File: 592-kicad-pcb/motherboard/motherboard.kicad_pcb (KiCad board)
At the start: 4 copper layers, 0 parts

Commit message: rough layout stufF
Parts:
- added C1: 100n, Capacitor_SMD:C_0603_1608Metric, F.Cu at (92.2, 148.4)
- added C10: 100n, Capacitor_SMD:C_0603_1608Metric, F.Cu at (91.0, 129.9)
- added C11: 100n, Capacitor_SMD:C_0603_1608Metric, F.Cu at (86.7, 129.9)
- added C2: 100n, Capacitor_SMD:C_0603_1608Metric, F.Cu at (103.0, 140.1)
- added C3: 1u, Capacitor_SMD:C_0603_1608Metric, F.Cu at (97.5, 137.8)
- added C5: 16p, Capacitor_SMD:C_0603_1608Metric, F.Cu at (86.7, 154.4)
- added C6: 16p, Capacitor_SMD:C_0603_1608Metric, F.Cu at (86.7, 157.6)
- added C7: 100n, Capacitor_SMD:C_0603_1608Metric, F.Cu at (87.2, 148.4)
- added C8: 1u 1206, Resistor_SMD:R_1206_3216Metric, F.Cu at (105.0, 114.0)
- added C9: 100n, Capacitor_SMD:C_0603_1608Metric, F.Cu at (99.0, 162.5)
- added J1: U.FL, Connector_Coaxial:U.FL_Hirose_U.FL-R-SMT-1_Vertical, F.Cu at (86.7, 138.9)
- added J2: U.FL, Connector_Coaxial:U.FL_Hirose_U.FL-R-SMT-1_Vertical, F.Cu at (102.0, 145.1)
- added J3: U.FL, Connector_Coaxial:U.FL_Hirose_U.FL-R-SMT-1_Vertical, F.Cu at (102.0, 135.1)
- added J4: Conn_02x06_Odd_Even, Connector_PinSocket_2.54mm:PinSocket_2x06_P2.54mm_Horizontal, B.Cu at (63.1, 125.8)
- added J5: Conn_02x06_Odd_Even, Connector_PinSocket_2.54mm:PinSocket_2x06_P2.54mm_Horizontal, B.Cu at (62.5, 148.6)
- added J6: 2.54mm jumper, Connector_PinHeader_2.54mm:PinHeader_1x03_P2.54mm_Vertical, F.Cu at (103.0, 121.5)
- added J7: Conn_02x06_Odd_Even, Connector_PinSocket_2.54mm:PinSocket_2x06_P2.54mm_Horizontal, B.Cu at (119.9, 134.7)
- added J8: Conn_02x06_Odd_Even, Connector_PinSocket_2.54mm:PinSocket_2x06_P2.54mm_Horizontal, B.Cu at (62.6, 169.3)
- added J9: Conn_02x06_Odd_Even, Connector_PinSocket_2.54mm:PinSocket_2x06_P2.54mm_Horizontal, B.Cu at (119.4, 155.2)
- added JP1: Jumper_2_Small_Bridged, Jumper:SolderJumper-2_P1.3mm_Bridged_RoundedPad1.0x1.5mm, F.Cu at (84.7, 154.2)
- added JP2: Jumper_2_Small_Bridged, Jumper:SolderJumper-2_P1.3mm_Bridged_RoundedPad1.0x1.5mm, F.Cu at (84.7, 157.8)
- added R1: 1M, Resistor_SMD:R_0603_1608Metric, F.Cu at (107.5, 136.1)
- added R10: 100k, Resistor_SMD:R_0603_1608Metric, F.Cu at (73.0, 122.0)
- added R11: 100k, Resistor_SMD:R_0603_1608Metric, F.Cu at (73.0, 124.5)
- added R12: 4k, Resistor_SMD:R_0603_1608Metric, F.Cu at (80.0, 166.5)
- added R13: 4k, Resistor_SMD:R_0603_1608Metric, F.Cu at (82.5, 166.5)
- added R14: 10k, Resistor_SMD:R_0603_1608Metric, F.Cu at (91.0, 127.9)
- added R15: 10k, Resistor_SMD:R_0603_1608Metric, F.Cu at (86.7, 127.9)
- added R16: 1M, Resistor_SMD:R_0603_1608Metric, F.Cu at (105.5, 127.7)
- added R17: 100k, Resistor_SMD:R_0603_1608Metric, F.Cu at (73.0, 127.0)
- added R18: 100k, Resistor_SMD:R_0603_1608Metric, F.Cu at (72.5, 114.5)
- added R19: 100k, Resistor_SMD:R_0603_1608Metric, F.Cu at (73.2, 141.0)
- added R2: 1M, Resistor_SMD:R_0603_1608Metric, F.Cu at (107.5, 144.1)
- added R20: 4k, Resistor_SMD:R_0603_1608Metric, F.Cu at (85.0, 166.5)
- added R21: 100k, Resistor_SMD:R_0603_1608Metric, F.Cu at (87.5, 166.5)
- added R22: 100k, Resistor_SMD:R_0603_1608Metric, F.Cu at (90.0, 166.5)
- added R23: 100k, Resistor_SMD:R_0603_1608Metric, F.Cu at (73.2, 143.5)
- added R24: 100k, Resistor_SMD:R_0603_1608Metric, F.Cu at (73.2, 146.0)
- added R25: 4k, Resistor_SMD:R_0603_1608Metric, F.Cu at (92.5, 166.5)
- added R26: 100k, Resistor_SMD:R_0603_1608Metric, F.Cu at (73.2, 148.5)
- added R27: 100k, Resistor_SMD:R_0603_1608Metric, F.Cu at (72.7, 136.5)
- added R28: 1M, Resistor_SMD:R_0603_1608Metric, F.Cu at (113.2, 142.0)
- added R29: 1M, Resistor_SMD:R_0603_1608Metric, F.Cu at (113.2, 139.5)
- added R3: 10, Resistor_SMD:R_0603_1608Metric, F.Cu at (87.7, 143.4)
- added R32: 100k, Resistor_SMD:R_0603_1608Metric, F.Cu at (89.7, 138.4)
- added R4: 10, Resistor_SMD:R_0603_1608Metric, F.Cu at (89.7, 143.4)
- added R5: 10, Resistor_SMD:R_0603_1608Metric, F.Cu at (92.2, 144.9)
- added R6: 10k, Resistor_SMD:R_0603_1608Metric, F.Cu at (104.5, 118.5)
- added R7: 10k, Resistor_SMD:R_0603_1608Metric, F.Cu at (99.0, 159.0)
- added R8: 100k, Resistor_SMD:R_0603_1608Metric, F.Cu at (72.5, 118.0)
- added R9: 100k, Resistor_SMD:R_0603_1608Metric, F.Cu at (72.8, 139.0)
- added SW1: C318884, Button_Switch_SMD:SW_Push_1P1T_XKB_TS-1187A, F.Cu at (103.0, 161.5)
- added U1: SN74LVC1G3157DBVR, Package_TO_SOT_SMD:SOT-23-6, F.Cu at (86.7, 133.9)
- added U2: SMXS-04K, 592-partslib:SMXS-04K-TP, F.Cu at (88.2, 120.4)
- added U3: SN74LVC1G3157DBVR, Package_TO_SOT_SMD:SOT-23-6, F.Cu at (91.1, 134.0)
- added U4: OPA2328DR, Package_SO:VSSOP-8_3x3mm_P0.65mm, F.Cu at (105.5, 140.1)
- added U5: 74LVC1T45GW, Package_TO_SOT_SMD:SOT-363_SC-70-6, F.Cu at (103.2, 127.6)
- added U6: 74LVC1T45GW, Package_TO_SOT_SMD:SOT-363_SC-70-6, F.Cu at (104.6, 154.9)
- added U8: 74LVC1T45GW, Package_TO_SOT_SMD:SOT-363_SC-70-6, F.Cu at (92.2, 138.4)
- added U9: SN74LVC1G14DBV, Package_TO_SOT_SMD:SOT-23-5, F.Cu at (101.0, 155.0)
- added Y1: Si5351A, Package_SO:MSOP-10_3x3mm_P0.5mm, F.Cu at (89.7, 148.4)
- added Y2: NX3225GA-25.000M-STD-CRG-2, Crystal:Crystal_SMD_3225-4Pin_3.2x2.5mm, F.Cu at (89.3, 155.0)
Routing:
- net /CHIP_FS_EXT: track 0.00 -> 12.1 mm
- net /clock_sources/FS_EXT_GEN: track 0.00 -> 9.81 mm
- net /MCU_GPIO_FS_SEL: track 0.00 -> 8.94 mm
- net /MCU_GPIO_NFCCLK_SEL: track 0.00 -> 8.85 mm
- net /CHIP_ext_clk_dig: track 0.00 -> 8.37 mm
- net /ANA_MUX_OUT_2_BUF: track 0.00 -> 5.11 mm
- net /ANA_MUX_OUT_1_BUF: track 0.00 -> 4.15 mm
- net /clock_sources/FS_EXT_AUX: track 0.00 -> 3.90 mm
- net Net-(Y1-CLK0): track 0.00 -> 2.48 mm
- net Net-(Y1-CLK1): track 0.00 -> 2.27 mm
- net /clock_sources/EXT_CLK_DIG_GEN: track 0.00 -> 1.79 mm
- net /CHIP_NFC_AFE_TDO_EXT: track 0.00 -> 1.77 mm

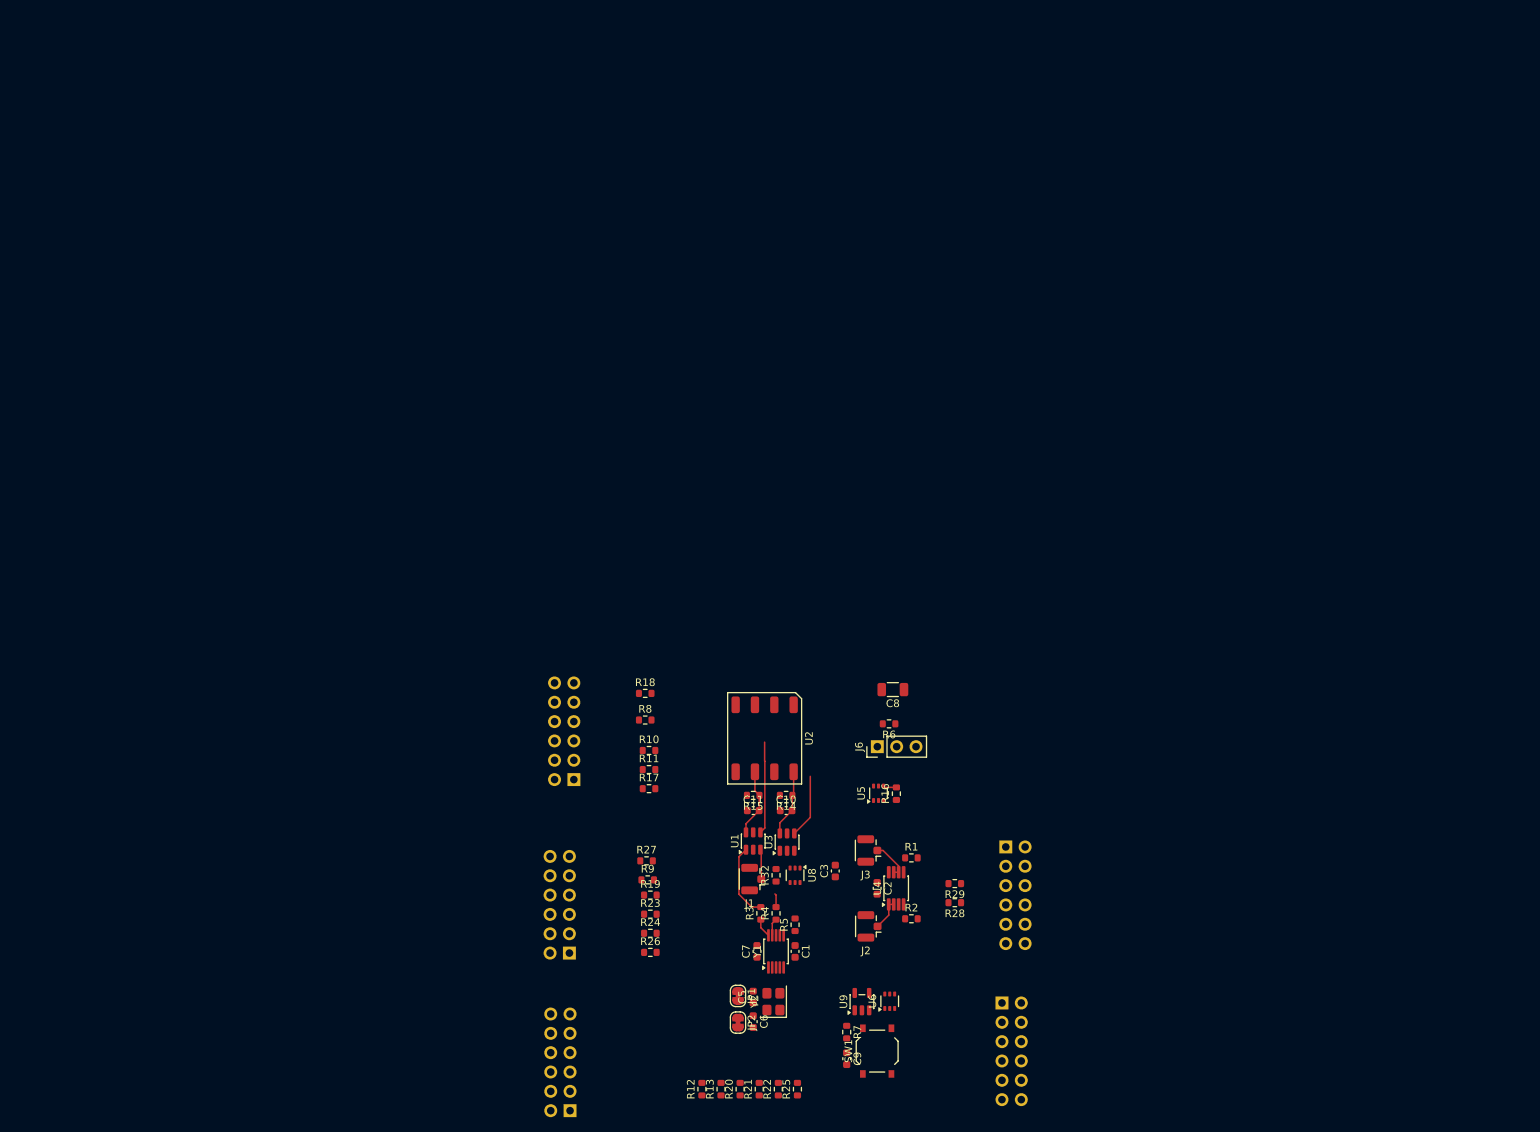
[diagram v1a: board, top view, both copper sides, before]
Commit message: add JLC part num for parts, footprints
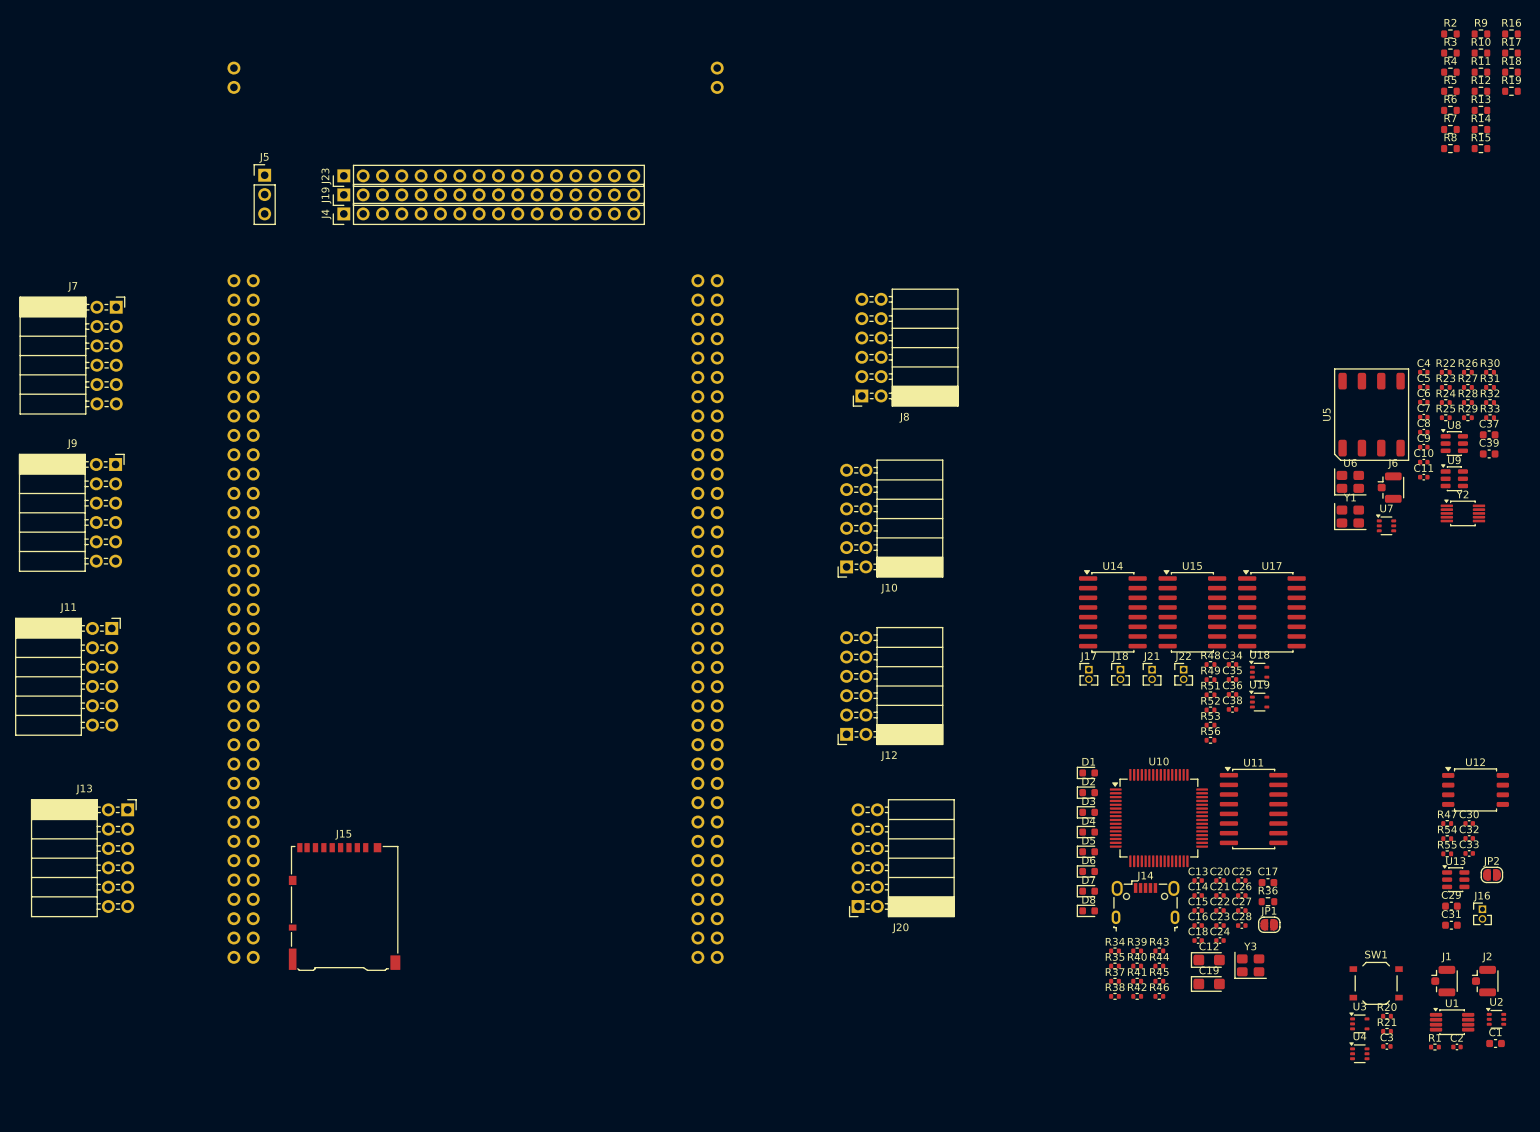
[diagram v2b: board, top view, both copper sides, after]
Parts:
- removed J3: U.FL, Connector_Coaxial:U.FL_Hirose_U.FL-R-SMT-1_Vertical
- added C12: 4.7u, Capacitor_Tantalum_SMD:CP_EIA-3216-18_Kemet-A, F.Cu at (146.6, 149.5)
- added C13: 10p, Capacitor_SMD:C_0402_1005Metric, F.Cu at (145.1, 139.1)
- added C14: 10p, Capacitor_SMD:C_0402_1005Metric, F.Cu at (145.1, 141.1)
- added C15: 100n, Capacitor_SMD:C_0402_1005Metric, F.Cu at (145.1, 143.0)
- added C16: 100n, Capacitor_SMD:C_0402_1005Metric, F.Cu at (145.1, 145.0)
- added C17: 3.3u, Capacitor_SMD:C_0603_1608Metric, F.Cu at (154.3, 139.4)
- added C18: 10n, Capacitor_SMD:C_0402_1005Metric, F.Cu at (145.1, 147.0)
- added C19: 4.7u, Capacitor_Tantalum_SMD:CP_EIA-3216-18_Kemet-A, F.Cu at (146.6, 152.7)
- added C20: 100n, Capacitor_SMD:C_0402_1005Metric, F.Cu at (148.0, 139.1)
- added C21: 100n, Capacitor_SMD:C_0402_1005Metric, F.Cu at (148.0, 141.1)
- added C22: 100n, Capacitor_SMD:C_0402_1005Metric, F.Cu at (148.0, 143.0)
- added C23: 100n, Capacitor_SMD:C_0402_1005Metric, F.Cu at (148.0, 145.0)
- added C24: 100n, Capacitor_SMD:C_0402_1005Metric, F.Cu at (148.0, 147.0)
- added C25: 100n, Capacitor_SMD:C_0402_1005Metric, F.Cu at (150.9, 139.1)
- added C26: 100n, Capacitor_SMD:C_0402_1005Metric, F.Cu at (150.9, 141.1)
- added C27: 100n, Capacitor_SMD:C_0402_1005Metric, F.Cu at (150.9, 143.0)
- added C28: 100n, Capacitor_SMD:C_0402_1005Metric, F.Cu at (150.9, 145.0)
- added C29: 1u, Capacitor_SMD:C_0603_1608Metric, F.Cu at (178.4, 142.4)
- added C30: 100n, Capacitor_SMD:C_0402_1005Metric, F.Cu at (180.8, 131.6)
- added C31: 1u, Capacitor_SMD:C_0603_1608Metric, F.Cu at (178.4, 145.0)
- added C32: 100n, Capacitor_SMD:C_0402_1005Metric, F.Cu at (180.8, 133.6)
- added C33: 100n, Capacitor_SMD:C_0402_1005Metric, F.Cu at (180.8, 135.5)
- added C34: 100n, Capacitor_SMD:C_0402_1005Metric, F.Cu at (149.7, 110.7)
- added C35: 100n, Capacitor_SMD:C_0402_1005Metric, F.Cu at (149.7, 112.7)
- added C36: 100n, Capacitor_SMD:C_0402_1005Metric, F.Cu at (149.7, 114.6)
- added C37: 1u, Capacitor_SMD:C_0603_1608Metric, F.Cu at (183.4, 80.5)
- added C38: 100n, Capacitor_SMD:C_0402_1005Metric, F.Cu at (149.7, 116.6)
- added C39: 1u, Capacitor_SMD:C_0603_1608Metric, F.Cu at (183.4, 83.0)
- added C4: 16p, Capacitor_SMD:C_0402_1005Metric, F.Cu at (174.8, 72.3)
- added D1: d_white, Diode_SMD:D_0603_1608Metric, F.Cu at (130.8, 125.0)
- added D2: d_white, Diode_SMD:D_0603_1608Metric, F.Cu at (130.8, 127.5)
- added D3: d_white, Diode_SMD:D_0603_1608Metric, F.Cu at (130.8, 130.1)
- added D4: d_white, Diode_SMD:D_0603_1608Metric, F.Cu at (130.8, 132.7)
- added D5: d_red, Diode_SMD:D_0603_1608Metric, F.Cu at (130.8, 135.3)
- added D6: d_red, Diode_SMD:D_0603_1608Metric, F.Cu at (130.8, 137.9)
- added D7: d_red, Diode_SMD:D_0603_1608Metric, F.Cu at (130.8, 140.5)
- added D8: d_red, Diode_SMD:D_0603_1608Metric, F.Cu at (130.8, 143.1)
- added J10: Conn_02x06_Odd_Even, Connector_PinSocket_2.54mm:PinSocket_2x06_P2.54mm_Horizontal, F.Cu at (99.0, 97.9)
- added J11: Conn_02x06_Odd_Even, Connector_PinSocket_2.54mm:PinSocket_2x06_P2.54mm_Horizontal, F.Cu at (2.42, 106.0)
- added J12: Conn_02x06_Odd_Even, Connector_PinSocket_2.54mm:PinSocket_2x06_P2.54mm_Horizontal, F.Cu at (99.0, 119.9)
- added J13: Conn_02x06_Odd_Even, Connector_PinSocket_2.54mm:PinSocket_2x06_P2.54mm_Horizontal, F.Cu at (4.50, 129.8)
- added J14: USB_B_Micro, Connector_USB:USB_Micro-B_Wuerth_629105150521, F.Cu at (138.2, 142.0)
- added J15: Micro_SD_Card, Connector_Card:microSD_HC_Hirose_DM3AT-SF-PEJM5, F.Cu at (33.0, 142.5)
- added J16: Conn_02x01, Connector_PinHeader_1.27mm:PinHeader_1x02_P1.27mm_Vertical, F.Cu at (182.5, 142.9)
- added J17: Conn_02x01, Connector_PinHeader_1.27mm:PinHeader_1x02_P1.27mm_Vertical, F.Cu at (130.8, 111.4)
- added J18: Conn_02x01, Connector_PinHeader_1.27mm:PinHeader_1x02_P1.27mm_Vertical, F.Cu at (134.9, 111.4)
- added J19: Conn_01x16, Connector_PinHeader_2.54mm:PinHeader_1x16_P2.54mm_Vertical, F.Cu at (32.9, 49.0)
- added J20: Conn_02x06_Odd_Even, Connector_PinSocket_2.54mm:PinSocket_2x06_P2.54mm_Horizontal, F.Cu at (100.5, 142.5)
- added J21: Conn_02x01, Connector_PinHeader_1.27mm:PinHeader_1x02_P1.27mm_Vertical, F.Cu at (139.1, 111.4)
- added J22: Conn_02x01, Connector_PinHeader_1.27mm:PinHeader_1x02_P1.27mm_Vertical, F.Cu at (143.2, 111.4)
- added J23: Conn_01x16, Connector_PinHeader_2.54mm:PinHeader_1x16_P2.54mm_Vertical, F.Cu at (32.9, 46.5)
- added R30: 10k, Resistor_SMD:R_0402_1005Metric, F.Cu at (183.5, 72.3)
- added R31: 10k, Resistor_SMD:R_0402_1005Metric, F.Cu at (183.5, 74.3)
- added R33: 10k, Resistor_SMD:R_0402_1005Metric, F.Cu at (183.5, 78.3)
- added R34: 4.7k, Resistor_SMD:R_0402_1005Metric, F.Cu at (134.2, 148.3)
- added R35: 10k, Resistor_SMD:R_0402_1005Metric, F.Cu at (134.2, 150.3)
- added R36: 12k <1%, Resistor_SMD:R_0603_1608Metric, F.Cu at (154.3, 141.9)
- added R37: 1k, Resistor_SMD:R_0402_1005Metric, F.Cu at (134.2, 152.3)
- added R38: 150, Resistor_SMD:R_0402_1005Metric, F.Cu at (134.2, 154.3)
- added R39: 150, Resistor_SMD:R_0402_1005Metric, F.Cu at (137.1, 148.3)
- added R40: 150, Resistor_SMD:R_0402_1005Metric, F.Cu at (137.1, 150.3)
- added R41: 150, Resistor_SMD:R_0402_1005Metric, F.Cu at (137.1, 152.3)
- added R42: 330, Resistor_SMD:R_0402_1005Metric, F.Cu at (137.1, 154.3)
- added R43: 330, Resistor_SMD:R_0402_1005Metric, F.Cu at (140.0, 148.3)
- added R44: 330, Resistor_SMD:R_0402_1005Metric, F.Cu at (140.0, 150.3)
- added R45: 330, Resistor_SMD:R_0402_1005Metric, F.Cu at (140.0, 152.3)
- added R46: 10k, Resistor_SMD:R_0402_1005Metric, F.Cu at (140.0, 154.3)
- added R47: 10k, Resistor_SMD:R_0402_1005Metric, F.Cu at (177.9, 131.6)
- added R48: 10k, Resistor_SMD:R_0402_1005Metric, F.Cu at (146.8, 110.7)
- added R49: 10k, Resistor_SMD:R_0402_1005Metric, F.Cu at (146.8, 112.7)
- added R51: 10k, Resistor_SMD:R_0402_1005Metric, F.Cu at (146.8, 114.7)
- added R52: 10k, Resistor_SMD:R_0402_1005Metric, F.Cu at (146.8, 116.7)
- added R53: 10k, Resistor_SMD:R_0402_1005Metric, F.Cu at (146.8, 118.7)
- added R54: 10k, Resistor_SMD:R_0402_1005Metric, F.Cu at (177.9, 133.6)
- added R55: 10k, Resistor_SMD:R_0402_1005Metric, F.Cu at (177.9, 135.6)
- added R56: 10k, Resistor_SMD:R_0402_1005Metric, F.Cu at (146.8, 120.7)
- added U10: FT4232H, Package_QFP:LQFP-64_10x10mm_P0.5mm, F.Cu at (140.0, 130.9)
- added U11: 74HC595, Package_SO:SOIC-16W_5.3x10.2mm_P1.27mm, F.Cu at (152.4, 129.7)
- added U12: W25Q32JVSS, Package_SO:SOIC-8_5.3x5.3mm_P1.27mm, F.Cu at (181.6, 127.2)
- added U13: SN74LVC1G3157DBVR, Package_TO_SOT_SMD:SOT-23-6, F.Cu at (179.0, 139.0)
- added U14: 74CBTLV3257, Package_SO:SOIC-16W_5.3x10.2mm_P1.27mm, F.Cu at (133.9, 103.8)
- added U15: 74CBTLV3257, Package_SO:SOIC-16W_5.3x10.2mm_P1.27mm, F.Cu at (144.4, 103.8)
- added U16: NUCLEO144-H743ZI, Module:ST_Morpho_Connector_144_STLink, B.Cu at (82.0, 60.3)
- added U17: 74CBTLV3257, Package_SO:SOIC-16W_5.3x10.2mm_P1.27mm, F.Cu at (154.8, 103.8)
- added U18: SN74LVC1G14DBV, Package_TO_SOT_SMD:SOT-353_SC-70-5, F.Cu at (153.2, 111.7)
- added U19: SN74LVC1G14DBV, Package_TO_SOT_SMD:SOT-353_SC-70-5, F.Cu at (153.2, 115.6)
- added U7: 74LVC1T45GW, Package_TO_SOT_SMD:SOT-363_SC-70-6, F.Cu at (169.9, 92.5)
- added Y3: X322512MSB4SI, Crystal:Crystal_SMD_3225-4Pin_3.2x2.5mm, F.Cu at (152.0, 150.2)
- C1: value 100n -> 1u
- C10, C2, C5, C7, C9: footprint Capacitor_SMD:C_0603_1608Metric -> Capacitor_SMD:C_0402_1005Metric
- C11: value 100n -> 10n; footprint Capacitor_SMD:C_0603_1608Metric -> Capacitor_SMD:C_0402_1005Metric
- C3: value 1u -> 100n; footprint Capacitor_SMD:C_0603_1608Metric -> Capacitor_SMD:C_0402_1005Metric
- C6: value 16p -> 100n; footprint Capacitor_SMD:C_0603_1608Metric -> Capacitor_SMD:C_0402_1005Metric
- C8: value 1u 1206 -> 100n; footprint Resistor_SMD:R_1206_3216Metric -> Capacitor_SMD:C_0402_1005Metric
- J4: value Conn_02x06_Odd_Even -> Conn_01x16; footprint Connector_PinSocket_2.54mm:PinSocket_2x06_P2.54mm_Horizontal -> Connector_PinHeader_2.54mm:PinHeader_1x16_P2.54mm_Vertical; moved to F.Cu
- J5: value Conn_02x06_Odd_Even -> 2.54mm jumper; footprint Connector_PinSocket_2.54mm:PinSocket_2x06_P2.54mm_Horizontal -> Connector_PinHeader_2.54mm:PinHeader_1x03_P2.54mm_Vertical; moved to F.Cu
- J6: value 2.54mm jumper -> U.FL; footprint Connector_PinHeader_2.54mm:PinHeader_1x03_P2.54mm_Vertical -> Connector_Coaxial:U.FL_Hirose_U.FL-R-SMT-1_Vertical
- J7, J8, J9: moved to F.Cu
- JP1, JP2: value Jumper_2_Small_Bridged -> solderjump; footprint Jumper:SolderJumper-2_P1.3mm_Bridged_RoundedPad1.0x1.5mm -> Jumper:SolderJumper-2_P1.3mm_Open_RoundedPad1.0x1.5mm
- R1, R21: footprint Resistor_SMD:R_0603_1608Metric -> Resistor_SMD:R_0402_1005Metric
- R10, R11, R17, R18, R19, R8, R9: value 100k -> 10k
- R12, R13: value 4k -> 10k
- R16: value 1M -> 10k
- R2: value 1M -> 10M
- R20: value 4k -> 10k; footprint Resistor_SMD:R_0603_1608Metric -> Resistor_SMD:R_0402_1005Metric
- R22, R23, R27, R32: value 100k -> 10k; footprint Resistor_SMD:R_0603_1608Metric -> Resistor_SMD:R_0402_1005Metric
- R24, R26: value 100k -> 10; footprint Resistor_SMD:R_0603_1608Metric -> Resistor_SMD:R_0402_1005Metric
- R25: value 4k -> 10; footprint Resistor_SMD:R_0603_1608Metric -> Resistor_SMD:R_0402_1005Metric
- R28, R29: value 1M -> 10k; footprint Resistor_SMD:R_0603_1608Metric -> Resistor_SMD:R_0402_1005Metric
- R3, R4, R5: value 10 -> 10M
- R6, R7: value 10k -> 2k
- U1: value SN74LVC1G3157DBVR -> OPA2328DGKR; footprint Package_TO_SOT_SMD:SOT-23-6 -> Package_SO:VSSOP-8_3x3mm_P0.65mm
- U2: value SMXS-04K -> 74LVC1T45GW; footprint 592-partslib:SMXS-04K-TP -> Package_TO_SOT_SMD:SOT-363_SC-70-6
- U3: value SN74LVC1G3157DBVR -> SN74LVC1G14DBV; footprint Package_TO_SOT_SMD:SOT-23-6 -> Package_TO_SOT_SMD:SOT-353_SC-70-5
- U4: value OPA2328DR -> 74LVC1T45GW; footprint Package_SO:VSSOP-8_3x3mm_P0.65mm -> Package_TO_SOT_SMD:SOT-363_SC-70-6
- U5: value 74LVC1T45GW -> SMXS-04K; footprint Package_TO_SOT_SMD:SOT-363_SC-70-6 -> 592-partslib:SMXS-04K-TP
- U6: value 74LVC1T45GW -> SX3M10.000B10F20TNN; footprint Package_TO_SOT_SMD:SOT-363_SC-70-6 -> Crystal:Crystal_SMD_3225-4Pin_3.2x2.5mm
- U8: value 74LVC1T45GW -> SN74LVC1G3157DBVR; footprint Package_TO_SOT_SMD:SOT-363_SC-70-6 -> Package_TO_SOT_SMD:SOT-23-6
- U9: value SN74LVC1G14DBV -> SN74LVC1G3157DBVR; footprint Package_TO_SOT_SMD:SOT-23-5 -> Package_TO_SOT_SMD:SOT-23-6
- Y1: value Si5351A -> NX3225GA-25.000M-STD-CRG-2; footprint Package_SO:MSOP-10_3x3mm_P0.5mm -> Crystal:Crystal_SMD_3225-4Pin_3.2x2.5mm
- Y2: value NX3225GA-25.000M-STD-CRG-2 -> Si5351A; footprint Crystal:Crystal_SMD_3225-4Pin_3.2x2.5mm -> Package_SO:MSOP-10_3x3mm_P0.5mm
- moved R12 166.3 mm to (182.3, 35.4), turned to 0 degrees
- moved R13 162.8 mm to (182.3, 37.9), turned to 0 degrees
- moved R9 156.0 mm to (182.3, 27.9)
- moved R19 154.8 mm to (186.3, 35.4)
- moved R17 148.9 mm to (186.3, 30.4)
- moved R3 144.9 mm to (178.3, 30.4), turned to 0 degrees
- moved R7 142.7 mm to (178.3, 40.4), turned to 0 degrees
- moved R10 142.6 mm to (182.3, 30.4)
- moved R11 142.6 mm to (182.3, 32.9)
- moved R4 141.7 mm to (178.3, 32.9), turned to 0 degrees
- moved R18 140.1 mm to (186.3, 32.9)
- moved R5 139.3 mm to (178.3, 35.4), turned to 0 degrees
- moved J7 136.7 mm to (3.00, 63.8), turned to 0 degrees
- moved J9 136.3 mm to (2.92, 84.4), turned to 0 degrees
- moved R2 136.1 mm to (178.3, 27.9)
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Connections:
- C1 pad 1: +1V8 -> +3V3
- C10 pad 2: /MCU_GPIO_NFCCLK_SEL -> /motherboard_top/clock_sources/FS_EXT_SEL
- C11 pad 1: GND -> +3V3
- C11 pad 2: /MCU_GPIO_FS_SEL -> GND
- C3 pad 1: +3V3 -> /motherboard_top/chip_support_misc/GPIO_RESET_EXT
- C5 pad 1: Net-(JP1-B) -> Net-(Y2-XB)
- C6 pad 1: Net-(JP2-A) -> +3V3
- C7 pad 1: +3V3 -> GND
- C7 pad 2: GND -> /motherboard_top/clock_sources/EXT_CLK_DIG_SEL
- C8 pad 1: /CHIP_VRECT_OUT_EXT -> +1V8
- C9 pad 1: /MCU_GPIO_RESET_AFE -> GND
- C9 pad 2: GND -> /motherboard_top/clock_sources/CARAVEL_CLK_SEL
- J1 pad 1: /clock_sources/FS_EXT_AUX -> /motherboard_top/ADC_chip_ana_mux_out_1
- J2 pad 1: /ANA_MUX_OUT_1_BUF -> /motherboard_top/ADC_chip_ana_mux_out_2
- J4 pad 1: /CHIP_TRST_EXT -> /motherboard_top/mgmt_debug
- J4 pad 10: GND -> /motherboard_top/chip_connection/MGMT_flash2_sck
- J4 pad 11: +3V3 -> /motherboard_top/chip_connection/MGMT_flash2_io0
- J4 pad 12: GND -> /motherboard_top/chip_connection/MGMT_flash2_io1
- J4 pad 2: /CHIP_TMS_EXT -> /motherboard_top/mgmt_sdo
- J4 pad 3: /CHIP_TCK_EXT -> /motherboard_top/mgmt_sdi
- J4 pad 4: /CHIP_TDI_EXT -> /motherboard_top/mgmt_csb
- J4 pad 5: /CHIP_tdo -> /motherboard_top/mgmt_sck
- J4 pad 6: /CHIP_tdo2 -> /motherboard_top/UART_mgmt_uart_rx
- J4 pad 7: /CHIP_ext_reset_dig -> /motherboard_top/UART_mgmt_uart_tx
- J4 pad 8: GND -> /motherboard_top/chip_connection/MGMT_irq
- J4 pad 9: GND -> /motherboard_top/chip_connection/MGMT_flash2_csb
- J5 pad 1: /CHIP_jtag_TDO -> /motherboard_top/anamisc_vref_ext_in
- J5 pad 2: /CHIP_jtag_TMS -> /motherboard_top/chip_nfc_vref
- J5 pad 3: /CHIP_jtag_TCK -> /motherboard_top/chip_support_misc/VREF_DAC_OUT
- J6 pad 1: /VREF_EXT_IN -> /motherboard_top/clock_sources/fs_ext_aux
- J6 pad 2: /CHIP_VREF_EXT -> GND
- J7 pad 1: /CHIP_i2c_0_sda -> +1V8
- J7 pad 10: /VREF_EXT_IN -> GND
- J7 pad 12: GND -> +3V3
- J7 pad 2: /ANA_MUX_OUT_1_BUF -> /motherboard_top/anamisc_vref_ext_in
- J7 pad 3: /CHIP_i2c_0_scl -> /motherboard_top/ADC_chip_ana_mux_out_1
- J7 pad 4: /ANA_MUX_OUT_2_BUF -> /motherboard_top/chip_nfc_jtag_tdi
- J7 pad 5: GND -> /motherboard_top/ADC_chip_ana_mux_out_2
- J7 pad 6: /NFC_AFE_TDO_EXT_BUF -> /motherboard_top/GPIO_chip_nfc_ext_reset_dig
- J7 pad 7: GND -> /motherboard_top/GPIO_chip_nfc_afe_tdo_ext
- J7 pad 8: /CHIP_VRECT_OUT_EXT -> /motherboard_top/chip_nfc_vrect_out
- J7 pad 9: +1V8 -> GND
- J8 pad 1: unconnected-(J8-Pin_1-Pad1) -> /motherboard_top/rck_mem_cs
- J8 pad 10: unconnected-(J8-Pin_10-Pad10) -> GND
- J8 pad 11: unconnected-(J8-Pin_11-Pad11) -> +3V3
- J8 pad 12: unconnected-(J8-Pin_12-Pad12) -> +3V3
- J8 pad 3: unconnected-(J8-Pin_3-Pad3) -> /motherboard_top/rck_mem_mosi_io0
- J8 pad 5: unconnected-(J8-Pin_5-Pad5) -> /motherboard_top/rck_mem_miso_i01
- J8 pad 6: unconnected-(J8-Pin_6-Pad6) -> /motherboard_top/rck_mem_io2
- J8 pad 7: unconnected-(J8-Pin_7-Pad7) -> /motherboard_top/rck_mem_sck
- J8 pad 8: unconnected-(J8-Pin_8-Pad8) -> /motherboard_top/rck_mem_io3
- J8 pad 9: unconnected-(J8-Pin_9-Pad9) -> GND
- J9 pad 1: /debug_headers/DAT1 -> /motherboard_top/mgmt_csb
- J9 pad 2: /CHIP_spi_flash_0_cs_0 -> /motherboard_top/mgmt_debug
- J9 pad 3: /debug_headers/DAT2 -> /motherboard_top/mgmt_sdi
- J9 pad 4: /debug_headers/MOSI -> unconnected-(J9-Pin_4-Pad4)
- J9 pad 5: /debug_headers/CD -> /motherboard_top/mgmt_sdo
- J9 pad 6: /debug_headers/MISO -> /motherboard_top/UART_mgmt_uart_tx
- J9 pad 7: unconnected-(J9-Pin_7-Pad7) -> /motherboard_top/mgmt_sck
- J9 pad 8: /CHIP_spi_flash_0_sck -> /motherboard_top/UART_mgmt_uart_rx
- JP1 pad 2: Net-(JP1-B) -> Net-(J14-Shield)
- JP2 pad 1: Net-(JP2-A) -> GND
- JP2 pad 2: GND -> Net-(J15-SHIELD)
- R1 pad 1: /CHIP_ANA_MUX_OUT_2_EXT -> GND
- R1 pad 2: GND -> /motherboard_top/chip_nfc_nfc_afe_tdo
- R10 pad 1: /CHIP_ext_reset_dig -> +3V3
- R10 pad 2: GND -> /motherboard_top/chip_connection/resetb
- R11 pad 1: /CHIP_TDI_EXT -> /motherboard_top/GPIO_chip_nfc_ext_reset_dig
- R12 pad 1: +3V3 -> /motherboard_top/GPIO_chip_rck_reset_io
- R12 pad 2: /MCU_SCL -> GND
- R13 pad 1: /MCU_SDA -> +3V3
- R13 pad 2: +3V3 -> /motherboard_top/chip_nfc_jtag_tms
- R14 pad 1: /MCU_GPIO_NFCCLK_SEL -> /motherboard_top/chip_nfc_jtag_trst
- R14 pad 2: +3V3 -> GND
- R15 pad 1: /MCU_GPIO_FS_SEL -> /motherboard_top/chip_nfc_jtag_tdi
- R15 pad 2: +3V3 -> GND
- R16 pad 1: GND -> /motherboard_top/chip_nfc_jtag_tck
- R16 pad 2: /CHIP_NFC_AFE_TDO_EXT -> GND
- R17 pad 1: /CHIP_TMS_EXT -> +3V3
- R17 pad 2: GND -> /motherboard_top/chip_rck_jtag_tms
- R18 pad 1: /CHIP_TRST_EXT -> /motherboard_top/chip_rck_jtag_tdi
- R19 pad 1: /CHIP_spi_0_sck -> /motherboard_top/chip_rck_jtag_tck
- R2 pad 1: /CHIP_ANA_MUX_OUT_EXT -> /motherboard_top/chip_nfc_vrect_out
- R20 pad 2: /CHIP_i2c_0_sda -> /motherboard_top/chip_support_misc/GPIO_RESET_EXT
- R21 pad 1: +3V3 -> /motherboard_top/chip_nfc_vref
- R21 pad 2: /CHIP_spi_flash_0_cs_0 -> GND
- R22 pad 1: +3V3 -> /motherboard_top/clock_sources/EXT_CLK_DIG_SEL
- R22 pad 2: /CHIP_spi_0_cs_0 -> +3V3
- R23 pad 1: /CHIP_jtag_TDO -> /motherboard_top/clock_sources/CARAVEL_CLK_SEL
- R23 pad 2: GND -> +3V3
- R24 pad 1: /CHIP_jtag_TCK -> Net-(Y2-CLK0)
- R24 pad 2: GND -> /motherboard_top/clock_sources/fs_ext_gen
- R25 pad 1: /CHIP_i2c_0_scl -> Net-(Y2-CLK1)
- R25 pad 2: +3V3 -> /motherboard_top/clock_sources/ext_clk_dig_gen
- R26 pad 1: /CHIP_jtag_TDI -> Net-(Y2-CLK2)
- R26 pad 2: GND -> /motherboard_top/chip_rck_clock_uncore
- R27 pad 1: /CHIP_jtag_TMS -> GND
- R27 pad 2: GND -> /motherboard_top/chip_rck_clock_uncore
- R28 pad 1: /VREF_EXT_IN -> GND
- R28 pad 2: GND -> /motherboard_top/clock_sources/ext_clk_dig_gen
- R29 pad 1: /CHIP_VRECT_OUT_EXT -> /motherboard_top/clock_sources/FS_EXT_SEL
- R29 pad 2: GND -> +3V3
- R3 pad 1: Net-(Y1-CLK0) -> /motherboard_top/chip_nfc_ana_mux_out_2
- R3 pad 2: /clock_sources/FS_EXT_GEN -> GND
- R32 pad 1: /clock_sources/FS_EXT_AUX -> GND
- R32 pad 2: GND -> /motherboard_top/clock_sources/fs_ext_aux
- R4 pad 1: Net-(Y1-CLK1) -> /motherboard_top/chip_nfc_nfc_afe_tdo
- R4 pad 2: /clock_sources/EXT_CLK_DIG_GEN -> GND
- R5 pad 1: Net-(Y1-CLK2) -> /motherboard_top/chip_nfc_ana_mux_out
- R5 pad 2: /CHIP_clock_uncore -> GND
- R6 pad 1: /CHIP_VREF_EXT -> +3V3
- R6 pad 2: GND -> /motherboard_top/chip_rck_i2c_sda
- R7 pad 2: /MCU_GPIO_RESET_AFE -> /motherboard_top/chip_rck_i2c_scl
- R8 pad 1: /CHIP_TCK_EXT -> +3V3
- R8 pad 2: GND -> /motherboard_top/chip_rck_spi_0_cs_0
- R9 pad 1: /CHIP_reset_io -> +3V3
- R9 pad 2: GND -> /motherboard_top/chip_spi_flash_0_cs_0
- SW1 pad 1: /MCU_GPIO_RESET_AFE -> /motherboard_top/chip_support_misc/GPIO_RESET_EXT
- U1 pad 1: /clock_sources/FS_EXT_GEN -> /motherboard_top/ADC_chip_ana_mux_out_1
- U1 pad 2: GND -> /motherboard_top/ADC_chip_ana_mux_out_1
- U1 pad 3: /clock_sources/FS_EXT_AUX -> /motherboard_top/chip_nfc_ana_mux_out
- U1 pad 4: /CHIP_FS_EXT -> GND
- U1 pad 5: +3V3 -> /motherboard_top/chip_nfc_ana_mux_out_2
- U1 pad 6: /MCU_GPIO_FS_SEL -> /motherboard_top/ADC_chip_ana_mux_out_2
- U2 pad 1: GND -> +3V3
- U2 pad 3: GND -> /motherboard_top/GPIO_chip_nfc_afe_tdo_ext
- U2 pad 4: GND -> /motherboard_top/chip_nfc_nfc_afe_tdo
- U2 pad 6: /MCU_GPIO_FS_SEL -> +1V8
- U3 pad 1: Net-(U3-B2) -> unconnected-(U3-NC-Pad1)
- U3 pad 2: GND -> /motherboard_top/chip_support_misc/GPIO_RESET_EXT
- U3 pad 3: /MCU_TIM_NFCCLK -> GND
- U3 pad 4: /CHIP_ext_clk_dig -> Net-(U4-B)
- U4 pad 1: /ANA_MUX_OUT_1_BUF -> +1V8
- U4 pad 2: /ANA_MUX_OUT_1_BUF -> GND
- U4 pad 3: /CHIP_ANA_MUX_OUT_EXT -> /motherboard_top/chip_nfc_reset
- U4 pad 4: GND -> Net-(U4-B)
- U4 pad 5: /CHIP_ANA_MUX_OUT_2_EXT -> GND
- U4 pad 6: /ANA_MUX_OUT_2_BUF -> +3V3
- U5 pad 1: +3V3 -> GND
- U5 pad 3: /NFC_AFE_TDO_EXT_BUF -> GND
- U5 pad 4: /CHIP_NFC_AFE_TDO_EXT -> GND
- U5 pad 6: +1V8 -> /motherboard_top/clock_sources/FS_EXT_SEL
- U6 pad 1: +1V8 -> /motherboard_top/clock_sources/CARAVEL_CLK_EN
- U6 pad 3: /CHIP_RESET_EXT -> /motherboard_top/mgmt_clk
- U6 pad 4: Net-(U6-B) -> +3V3
- U8 pad 1: +3V3 -> /motherboard_top/clock_sources/fs_ext_gen
- U8 pad 3: Net-(U3-B2) -> /motherboard_top/clock_sources/fs_ext_aux
- U8 pad 4: /clock_sources/EXT_CLK_DIG_GEN -> /motherboard_top/chip_nfc_fs
- U8 pad 5: GND -> +3V3
- U8 pad 6: +1V8 -> /motherboard_top/clock_sources/FS_EXT_SEL
- U9 pad 1: unconnected-(U9-NC-Pad1) -> Net-(U7-A)
- U9 pad 2: /MCU_GPIO_RESET_AFE -> GND
- U9 pad 3: GND -> /motherboard_top/clock_sources/CLK_DIG_GPIO_GEN
- U9 pad 4: Net-(U6-B) -> /motherboard_top/chip_nfc_ext_clk_dig
- Y1 pad 1: +3V3 -> Net-(Y2-XB)
- Y1 pad 2: Net-(Y1-XA) -> GND
- Y1 pad 3: Net-(Y1-XB) -> Net-(Y2-XA)
- Y1 pad 4: /MCU_SCL -> GND
- Y2 pad 1: Net-(Y1-XB) -> +3V3
- Y2 pad 2: Net-(JP1-B) -> Net-(Y2-XA)
- Y2 pad 3: Net-(Y1-XA) -> Net-(Y2-XB)
- Y2 pad 4: Net-(JP2-A) -> /motherboard_top/clock_sources/SCL
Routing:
- net /CHIP_FS_EXT: track 12.1 -> 0.00 mm
- net /clock_sources/FS_EXT_GEN: track 9.81 -> 0.00 mm
- net /MCU_GPIO_FS_SEL: track 8.94 -> 0.00 mm
- net /MCU_GPIO_NFCCLK_SEL: track 8.85 -> 0.00 mm
- net /CHIP_ext_clk_dig: track 8.37 -> 0.00 mm
- net /ANA_MUX_OUT_2_BUF: track 5.11 -> 0.00 mm
- net /ANA_MUX_OUT_1_BUF: track 4.15 -> 0.00 mm
- net /clock_sources/FS_EXT_AUX: track 3.90 -> 0.00 mm
- net Net-(Y1-CLK0): track 2.48 -> 0.00 mm
- net Net-(Y1-CLK1): track 2.27 -> 0.00 mm
- net /clock_sources/EXT_CLK_DIG_GEN: track 1.79 -> 0.00 mm
- net /CHIP_NFC_AFE_TDO_EXT: track 1.77 -> 0.00 mm

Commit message: messing around with floorplanning
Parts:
- moved J15 298.9 mm to (331.3, 161.6)
- moved R27 219.9 mm to (361.8, 199.0)
- moved R26 219.7 mm to (361.2, 197.2)
- moved C8 219.5 mm to (361.2, 196.0)
- moved R24 217.9 mm to (361.2, 193.8)
- moved R25 217.5 mm to (361.2, 195.0)
- moved R28 217.1 mm to (363.5, 193.2), turned to -90 degrees
- moved R30 214.4 mm to (361.2, 192.2)
- moved C37 214.2 mm to (364.2, 195.2)
- moved C6 213.8 mm to (353.8, 193.2), turned to 180 degrees
- moved Y1 212.1 mm to (349.6, 195.9)
- moved D7 212.0 mm to (331.3, 71.7), turned to -90 degrees
- moved D3 206.0 mm to (328.2, 71.5), turned to -90 degrees
- moved R40 205.7 mm to (328.3, 74.3), turned to -90 degrees
- moved R44 205.7 mm to (331.2, 74.5), turned to 90 degrees
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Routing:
- net /motherboard_top/clock_sources/ext_clk_dig_gen: track 0.00 -> 4.86 mm
- net /motherboard_top/clock_sources/fs_ext_gen: track 0.00 -> 3.01 mm
- net /motherboard_top/chip_rck_clock_uncore: track 0.00 -> 3.01 mm
- net Net-(Y2-CLK2): track 0.00 -> 2.19 mm
- net /motherboard_top/ftdi/USB_DM: track 0.00 -> 1.93 mm
- net /motherboard_top/ftdi/USB_DP: track 0.00 -> 1.90 mm

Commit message: update motherboard floorplanning
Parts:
- added J24: DF40C-40DP-0.4V(51), Connector_Hirose_DF40:Hirose_DF40C(2.0)-40DS-0.4V_2x20_P0.4mm, F.Cu at (151.8, 142.7)
- added J3: DF40C-40DP-0.4V(51), Connector_Hirose_DF40:Hirose_DF40C(2.0)-40DS-0.4V_2x20_P0.4mm, F.Cu at (151.8, 108.6)
- U11, U14, U15, U17: footprint Package_SO:SOIC-16W_5.3x10.2mm_P1.27mm -> Package_SO:SOIC-16_3.9x9.9mm_P1.27mm
- moved C37 227.9 mm to (139.8, 155.7), turned to 180 degrees
- moved R27 225.6 mm to (140.8, 153.6), turned to 90 degrees
- moved R28 225.5 mm to (140.8, 157.7), turned to 90 degrees
- moved R26 223.1 mm to (142.6, 153.1), turned to 180 degrees
- moved C8 222.6 mm to (142.5, 154.4), turned to 180 degrees
- moved R25 222.2 mm to (142.6, 155.7), turned to 180 degrees
- moved R24 221.8 mm to (142.6, 156.9), turned to 180 degrees
- moved R30 221.3 mm to (142.6, 158.2), turned to 180 degrees
- moved Y2 213.4 mm to (147.2, 155.2), turned to 180 degrees
- moved C39 209.7 mm to (146.1, 157.9)
- moved J15 208.4 mm to (168.3, 31.8), turned to 180 degrees
- moved C6 207.7 mm to (149.2, 157.4)
- moved C21 203.7 mm to (125.0, 46.4), turned to 0 degrees
- moved R33 202.2 mm to (135.1, 162.7), turned to -90 degrees
- moved R55 200.5 mm to (166.5, 41.8), turned to 90 degrees
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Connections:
- C9 pad 2: /motherboard_top/clock_sources/CARAVEL_CLK_SEL -> /motherboard_top/clock_sources/CARAVEL_CLK_EN
- R23 pad 1: /motherboard_top/clock_sources/CARAVEL_CLK_SEL -> /motherboard_top/clock_sources/CARAVEL_CLK_EN
- U5 pad 7: /motherboard_top/clock_sources/CARAVEL_CLK_SEL -> /motherboard_top/clock_sources/CARAVEL_CLK_EN
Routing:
- net /motherboard_top/clock_sources/ext_clk_dig_gen: track 4.86 -> 0.00 mm
- net /motherboard_top/clock_sources/fs_ext_gen: track 3.01 -> 0.00 mm
- net /motherboard_top/chip_rck_clock_uncore: track 3.01 -> 0.00 mm
- net Net-(Y2-CLK2): track 2.19 -> 0.00 mm
- net /motherboard_top/ftdi/USB_DM: track 1.93 -> 0.00 mm
- net /motherboard_top/ftdi/USB_DP: track 1.90 -> 0.00 mm
